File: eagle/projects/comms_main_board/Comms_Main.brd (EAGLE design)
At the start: 101.6 x 95.2 mm, 195 parts, among them J1 WRL-00593, J10 MOL-SL-2-RA, J11 MOL-SL-3-RA, J12 MOL-SL-3-RA, J13 MOL-SL-3-RA, J14 MOL-SL-3-RA, J15 MOL-SL-2-RA, J16 MOL-MINIJR-2P-RA, J17 MOL-MINIJR-2P-RA, J18 MOL-MINIJR-2P-RA, J19 MOL-MINIJR-2P-RA, J2 PRT-12639, J20 MOL-SL-2-RA, J21 RECEPTACLE-2x2-254MM, J22 MOL-SL-2-RA, J3 PRT-12639, J4 PRT-12639, J5 PRT-12639, J6 MOL-SL-3-RA, J7 MOL-SL-5-RA, J8 RECEPTACLE-2x20-254MM, J9 MOL-SL-3-RA, Q1 CSD17579Q3A, U1 TPS562209DDCT, U10 MCP4541-103E/MS, U11 TPS562209DDCT, U12 MMBT3904-HF, U13 MAX3232CSE+, U14 MAX4311, U15 MAX6371, U16 2N7002P,215, U2 LP2985-33DBVR, U3 LP5900TLX-3.3/NOPB, U4 TPS562209DDCT, U5 NDT2955, U6 LM3488MMX/NOPB, U7 PCT2075D,118, U8 MS560702BA03-50, U9 MAX-M8Q

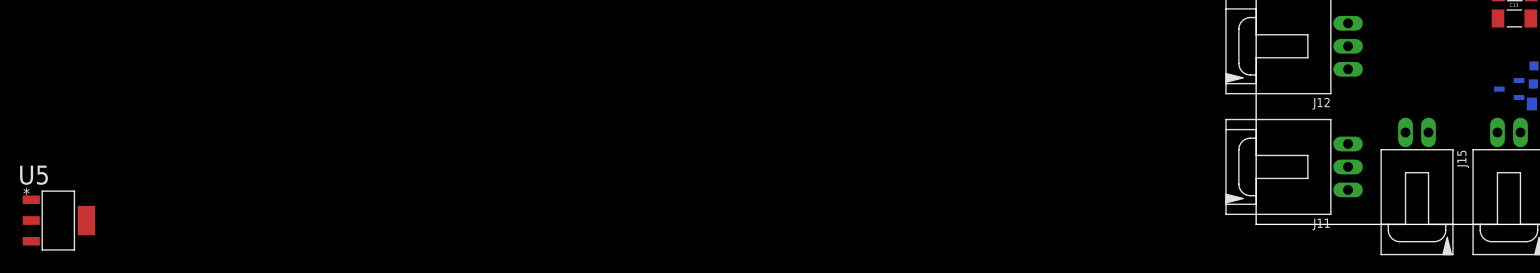
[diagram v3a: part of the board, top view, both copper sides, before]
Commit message: No-pop as assembly variant
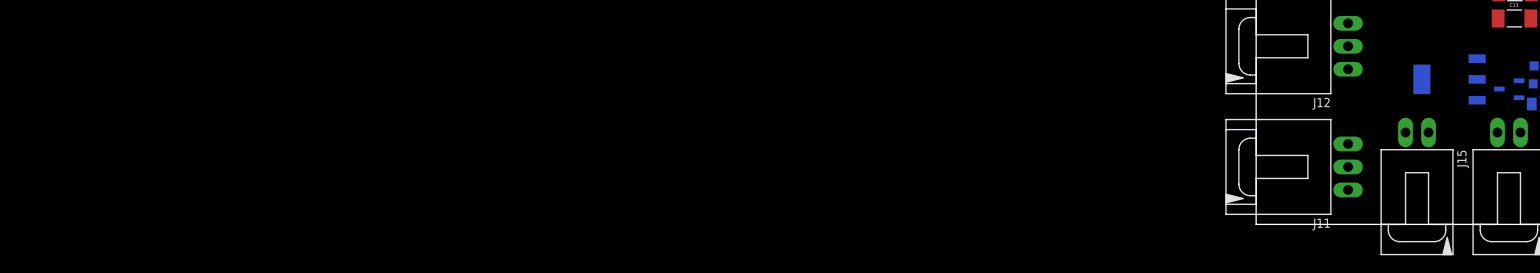
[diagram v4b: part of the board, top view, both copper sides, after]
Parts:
- moved U5 154.6 mm to (21.4, 16.0), flipped to the bottom
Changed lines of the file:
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@@
 </attributes>
 <variantdefs>
+<variantdef name="POR" current="yes"/>
 </variantdefs>
 <classes>
@@
 <attribute name="VENDOR" value="Digi-key" x="95.609096875" y="13.490184375" size="1.778" layer="28" rot="MR0" display="off"/>
 </element>
-<element name="R15" library="comms" package="R0603" value="0" x="95.6318625" y="15.678475" rot="MR0">
+<element name="R15" library="comms" package="R0603" value="0" x="95.6318625" y="15.678475" populate="no" rot="MR0">
 <attribute name="VENDOR_PN" value="P0.0GCT-ND" x="95.6318625" y="15.678475" size="1.778" layer="28" rot="MR0" display="off"/>
 <attribute name="MANUFACTURER_PN" value="ERJ-3GEY0R00V" x="95.6318625" y="15.678475" size="1.778" layer="28" rot="MR0" display="off"/>
@@
 <attribute name="VENDOR" value="Digi-key" x="32.831990625" y="28.757325" size="1.778" layer="27" display="off"/>
 </element>
-<element name="R20" library="comms" package="R0603" value="10k" x="31.856203125" y="76.851334375" rot="MR0">
+<element name="R20" library="comms" package="R0603" value="10k" x="31.856203125" y="76.851334375" populate="no" rot="MR0">
 <attribute name="VENDOR_PN" value="P10.0KHCT-ND" x="31.856203125" y="76.851334375" size="1.778" layer="28" rot="MR0" display="off"/>
 <attribute name="MANUFACTURER_PN" value="ERJ-3EKF1002V" x="31.856203125" y="76.851334375" size="1.778" layer="28" rot="MR0" display="off"/>
@@
 <attribute name="VENDOR" value="Digi-key" x="18.918459375" y="36.007771875" size="1.778" layer="28" rot="MR0" display="off"/>
 </element>
-<element name="R47" library="comms" package="R0603" value="0" x="18.70040625" y="40.48303125" rot="MR0">
+<element name="R47" library="comms" package="R0603" value="0" x="18.70040625" y="40.48303125" populate="no" rot="MR0">
 <attribute name="VENDOR_PN" value="P0.0GCT-ND" x="18.70040625" y="40.48303125" size="1.778" layer="28" rot="MR0" display="off"/>
 <attribute name="MANUFACTURER_PN" value="ERJ-3GEY0R00V" x="18.70040625" y="40.48303125" size="1.778" layer="28" rot="MR0" display="off"/>
@@
 <attribute name="VENDOR" value="Digi-key" x="18.992075" y="25.333253125" size="1.778" layer="28" rot="MR0" display="off"/>
 </element>
-<element name="R55" library="comms" package="R0805" value="0.0" x="39.84961875" y="68.887096875" rot="MR0">
+<element name="R55" library="comms" package="R0805" value="0.0" x="39.84961875" y="68.887096875" populate="no" rot="MR0">
 <attribute name="VENDOR_PN" value="P0.0ACT-ND" x="39.84961875" y="68.887096875" size="1.778" layer="28" rot="MR0" display="off"/>
 <attribute name="MANUFACTURER_PN" value="ERJ-6GEY0R00V" x="39.84961875" y="68.887096875" size="1.778" layer="28" rot="MR0" display="off"/>
@@
 <attribute name="VENDOR" value="Digi-Key" x="39.84961875" y="68.887096875" size="1.778" layer="28" rot="MR0" display="off"/>
 </element>
-<element name="R56" library="comms" package="R0805" value="0.0" x="54.45951875" y="69.015196875" rot="MR0">
+<element name="R56" library="comms" package="R0805" value="0.0" x="54.45951875" y="69.015196875" populate="no" rot="MR0">
 <attribute name="VENDOR_PN" value="P0.0ACT-ND" x="54.45951875" y="69.015196875" size="1.778" layer="28" rot="MR0" display="off"/>
 <attribute name="MANUFACTURER_PN" value="ERJ-6GEY0R00V" x="54.45951875" y="69.015196875" size="1.778" layer="28" rot="MR0" display="off"/>
@@
 <attribute name="VENDOR_PN" value="568-5818-1-ND" x="27.960040625" y="14.95311875" size="1.778" layer="28" rot="MR0" display="off"/>
 </element>
-<element name="R10" library="comms" package="R0805" value="0.0" x="31.463203125" y="13.299940625" rot="MR0">
+<element name="R10" library="comms" package="R0805" value="0.0" x="31.463203125" y="13.299940625" populate="no" rot="MR0">
 <attribute name="POWER" value="1/8W" x="31.463203125" y="13.299940625" size="1.778" layer="28" rot="MR0" display="off"/>
 <attribute name="VENDOR" value="Digi-Key" x="31.463203125" y="13.299940625" size="1.778" layer="28" rot="MR0" display="off"/>
@@
 <attribute name="VENDOR_PN" value="P0.0ACT-ND" x="31.463203125" y="13.299940625" size="1.778" layer="28" rot="MR0" display="off"/>
 </element>
-<element name="U5" library="comms" package="SOT230P700X180-4N" value="NDT2955" x="-132.375821875" y="0.4259625">
-<attribute name="VENDOR_PN" value="NDT2955CT-ND" x="-132.375821875" y="0.4259625" size="1.778" layer="27" display="off"/>
-<attribute name="VENDOR" value="Digi-Key" x="-132.375821875" y="0.4259625" size="1.778" layer="27" display="off"/>
-<attribute name="MANUFACTURER" value="Fairchild" x="-132.375821875" y="0.4259625" size="1.778" layer="27" display="off"/>
-<attribute name="MANUFACTURER_PN" value="NDT2955" x="-132.375821875" y="0.4259625" size="1.778" layer="27" display="off"/>
-<attribute name="PACKAGE" value="SOT-223-4" x="-132.375821875" y="0.4259625" size="1.778" layer="27" display="off"/>
+<element name="U5" library="comms" package="SOT230P700X180-4N" value="NDT2955" x="21.41910625" y="16.024090625" rot="MR0">
+<attribute name="VENDOR_PN" value="NDT2955CT-ND" x="21.41910625" y="16.024090625" size="1.778" layer="28" rot="MR0" display="off"/>
+<attribute name="VENDOR" value="Digi-Key" x="21.41910625" y="16.024090625" size="1.778" layer="28" rot="MR0" display="off"/>
+<attribute name="MANUFACTURER" value="Fairchild" x="21.41910625" y="16.024090625" size="1.778" layer="28" rot="MR0" display="off"/>
+<attribute name="MANUFACTURER_PN" value="NDT2955" x="21.41910625" y="16.024090625" size="1.778" layer="28" rot="MR0" display="off"/>
+<attribute name="PACKAGE" value="SOT-223-4" x="21.41910625" y="16.024090625" size="1.778" layer="28" rot="MR0" display="off"/>
 </element>
 </elements>
@@
 <contactref element="R8" pad="2"/>
 <contactref element="U5" pad="3"/>
-<wire x1="-24.13" y1="114.3" x2="-135.375821875" y2="-1.8740375" width="0" layer="19" extent="1-1"/>
-<wire x1="55.43383125" y1="59.4553" x2="-24.13" y2="114.3" width="0" layer="19" extent="1-1"/>
-<wire x1="65.582725" y1="55.370571875" x2="55.43383125" y2="59.4553" width="0" layer="19" extent="1-1"/>
-<wire x1="69.892540625" y1="54.175978125" x2="65.582725" y2="55.370571875" width="0" layer="19" extent="1-1"/>
+<wire x1="65.582725" y1="55.370571875" x2="69.892540625" y2="54.175978125" width="0" layer="19" extent="1-1"/>
+<wire x1="55.43383125" y1="59.4553" x2="65.582725" y2="55.370571875" width="0" layer="19" extent="1-1"/>
 <wire x1="71.755" y1="13.97" x2="69.892540625" y2="54.175978125" width="0" layer="19" extent="1-1"/>
 <wire x1="30.713996875" y1="17.52249375" x2="71.755" y2="13.97" width="0" layer="19" extent="16-16"/>
 <wire x1="30.463203125" y1="13.299940625" x2="30.713996875" y2="17.52249375" width="0" layer="19" extent="16-16"/>
+<wire x1="24.41910625" y1="13.724090625" x2="30.463203125" y2="13.299940625" width="0" layer="19" extent="16-16"/>
+<wire x1="-24.13" y1="114.3" x2="55.43383125" y2="59.4553" width="0" layer="19" extent="1-1"/>
 </signal>
 <signal name="DCDC_STEPUP_ISENSE_RES">
@@
 <contactref element="U5" pad="2"/>
 <contactref element="U5" pad="4"/>
-<wire x1="-129.275821875" y1="0.4259625" x2="-135.375821875" y2="0.4259625" width="0" layer="19" extent="1-1"/>
-<wire x1="32.463203125" y1="13.299940625" x2="-129.275821875" y2="0.4259625" width="0" layer="19" extent="1-16"/>
-<wire x1="39.37" y1="10.16" x2="32.463203125" y2="13.299940625" width="0" layer="19" extent="16-16"/>
+<wire x1="32.463203125" y1="13.299940625" x2="39.37" y2="10.16" width="0" layer="19" extent="16-16"/>
+<wire x1="24.41910625" y1="16.024090625" x2="32.463203125" y2="13.299940625" width="0" layer="19" extent="16-16"/>
+<wire x1="18.31910625" y1="16.024090625" x2="24.41910625" y2="16.024090625" width="0" layer="19" extent="16-16"/>
 </signal>
 <signal name="12V_PMOS_G">
@@
 <contactref element="U16" pad="3"/>
 <contactref element="U5" pad="1"/>
-<wire x1="26.867840625" y1="14.95311875" x2="-135.375821875" y2="2.7259625" width="0" layer="19" extent="1-16"/>
-<wire x1="32.413996875" y1="17.52249375" x2="26.867840625" y2="14.95311875" width="0" layer="19" extent="16-16"/>
+<wire x1="26.867840625" y1="14.95311875" x2="32.413996875" y2="17.52249375" width="0" layer="19" extent="16-16"/>
+<wire x1="24.41910625" y1="18.324090625" x2="26.867840625" y2="14.95311875" width="0" layer="19" extent="16-16"/>
 </signal>
 </signals>

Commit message: Changed WDT to be off 3.3V rail
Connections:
- net 3P3V_SENSORS: now also C36.1, R19.1, R20.2, U15.4, U15.5, U15.8
- net 5V_PI: no longer C36.1, R19.1, R20.2, U15.4, U15.5, U15.8
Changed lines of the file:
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@@
 <contactref element="U8" pad="2"/>
 <contactref element="R55" pad="2"/>
+<contactref element="U15" pad="5"/>
+<contactref element="U15" pad="4"/>
+<contactref element="U15" pad="8"/>
+<contactref element="C36" pad="1"/>
+<contactref element="R19" pad="1"/>
+<contactref element="R20" pad="2"/>
 <wire x1="57.640990625" y1="68.277221875" x2="57.216571875" y2="72.097946875" width="0" layer="19" extent="16-16"/>
 <wire x1="56.27350625" y1="66.3569625" x2="57.640990625" y2="68.277221875" width="0" layer="19" extent="16-16"/>
@@
 <wire x1="37.07379375" y1="69.094459375" x2="38.84961875" y2="68.887096875" width="0" layer="19" extent="16-16"/>
 <wire x1="37.07379375" y1="67.844459375" x2="37.07379375" y2="69.094459375" width="0" layer="19" extent="16-16"/>
+<wire x1="31.006203125" y1="76.851334375" x2="38.410153125" y2="71.502978125" width="0" layer="19" extent="16-16"/>
+<wire x1="29.3049625" y1="75.661178125" x2="31.006203125" y2="76.851334375" width="0" layer="19" extent="16-16"/>
+<wire x1="29.092090625" y1="73.712196875" x2="29.3049625" y2="75.661178125" width="0" layer="19" extent="16-16"/>
+<wire x1="26.9549625" y1="75.661178125" x2="29.3049625" y2="75.661178125" width="0" layer="19" extent="16-16"/>
+<wire x1="26.9549625" y1="77.611178125" x2="26.9549625" y2="75.661178125" width="0" layer="19" extent="16-16"/>
+<wire x1="32.644853125" y1="78.86829375" x2="31.006203125" y2="76.851334375" width="0" layer="19" extent="16-16"/>
 <wire x1="27.636603125" y1="54.31660625" x2="37.07379375" y2="67.844459375" width="0" layer="19" extent="16-16"/>
 <wire x1="28.364871875" y1="47.547296875" x2="27.636603125" y2="54.31660625" width="0" layer="19" extent="1-16"/>
@@
 </signal>
 <signal name="5V_PI">
-<contactref element="U15" pad="5"/>
-<contactref element="U15" pad="4"/>
-<contactref element="U15" pad="8"/>
-<contactref element="C36" pad="1"/>
-<contactref element="R19" pad="1"/>
-<contactref element="R20" pad="2"/>
 <contactref element="R1" pad="2"/>
 <contactref element="C3" pad="1"/>
@@
 <contactref element="J8" pad="2"/>
 <contactref element="J8" pad="4"/>
-<wire x1="31.006203125" y1="76.851334375" x2="32.644853125" y2="78.86829375" width="0" layer="19" extent="16-16"/>
-<wire x1="29.3049625" y1="75.661178125" x2="31.006203125" y2="76.851334375" width="0" layer="19" extent="16-16"/>
-<wire x1="29.092090625" y1="73.712196875" x2="29.3049625" y2="75.661178125" width="0" layer="19" extent="16-16"/>
-<wire x1="26.9549625" y1="75.661178125" x2="29.3049625" y2="75.661178125" width="0" layer="19" extent="16-16"/>
-<wire x1="26.9549625" y1="77.611178125" x2="26.9549625" y2="75.661178125" width="0" layer="19" extent="16-16"/>
-<wire x1="13.97" y1="86.36" x2="26.9549625" y2="77.611178125" width="0" layer="19" extent="16-16"/>
 <wire x1="11.43" y1="86.36" x2="13.97" y2="86.36" width="0" layer="19" extent="1-1"/>
-<wire x1="36.364071875" y1="33.68104375" x2="29.092090625" y2="73.712196875" width="0" layer="19" extent="1-16"/>
+<wire x1="36.364071875" y1="33.68104375" x2="13.97" y2="86.36" width="0" layer="19" extent="1-1"/>
 <wire x1="37.620825" y1="26.911371875" x2="36.364071875" y2="33.68104375" width="0" layer="19" extent="1-1"/>
 <wire x1="26.79621875" y1="25.651803125" x2="37.620825" y2="26.911371875" width="0" layer="19" extent="1-1"/>

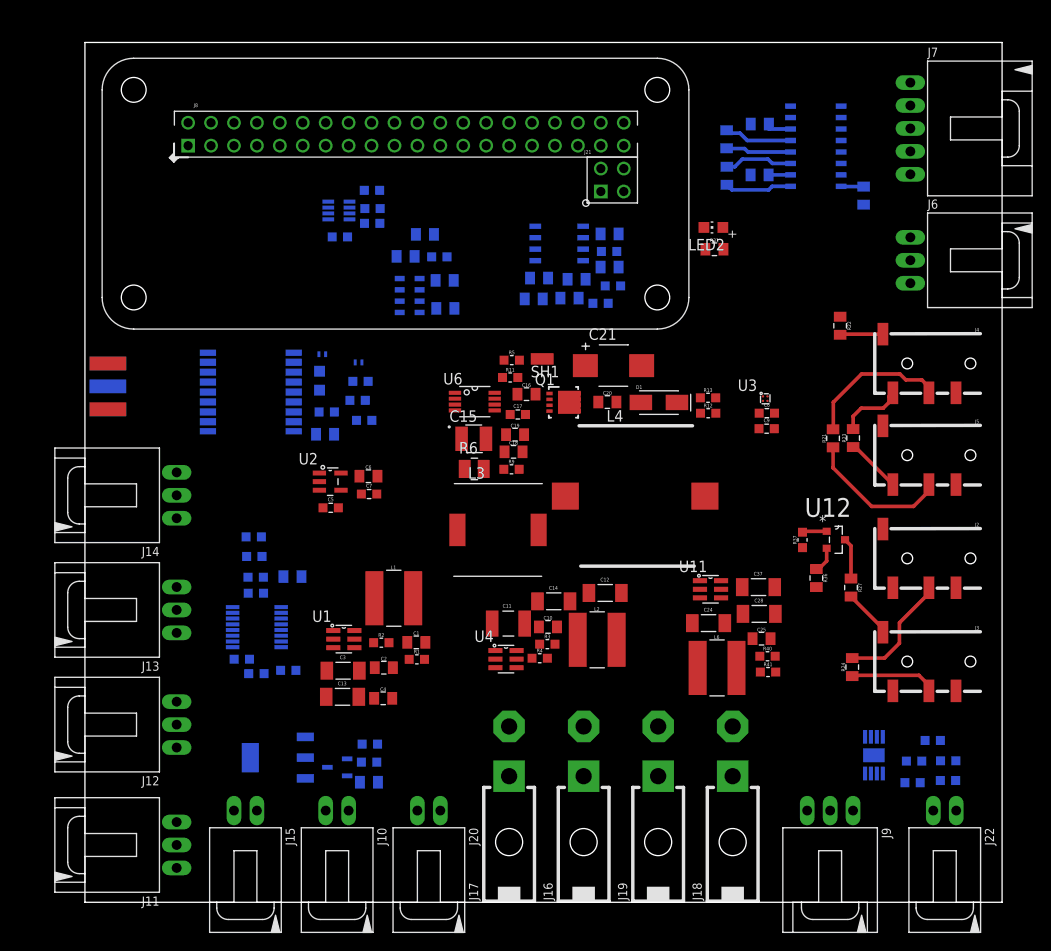
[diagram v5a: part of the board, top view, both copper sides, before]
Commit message: Update inductor
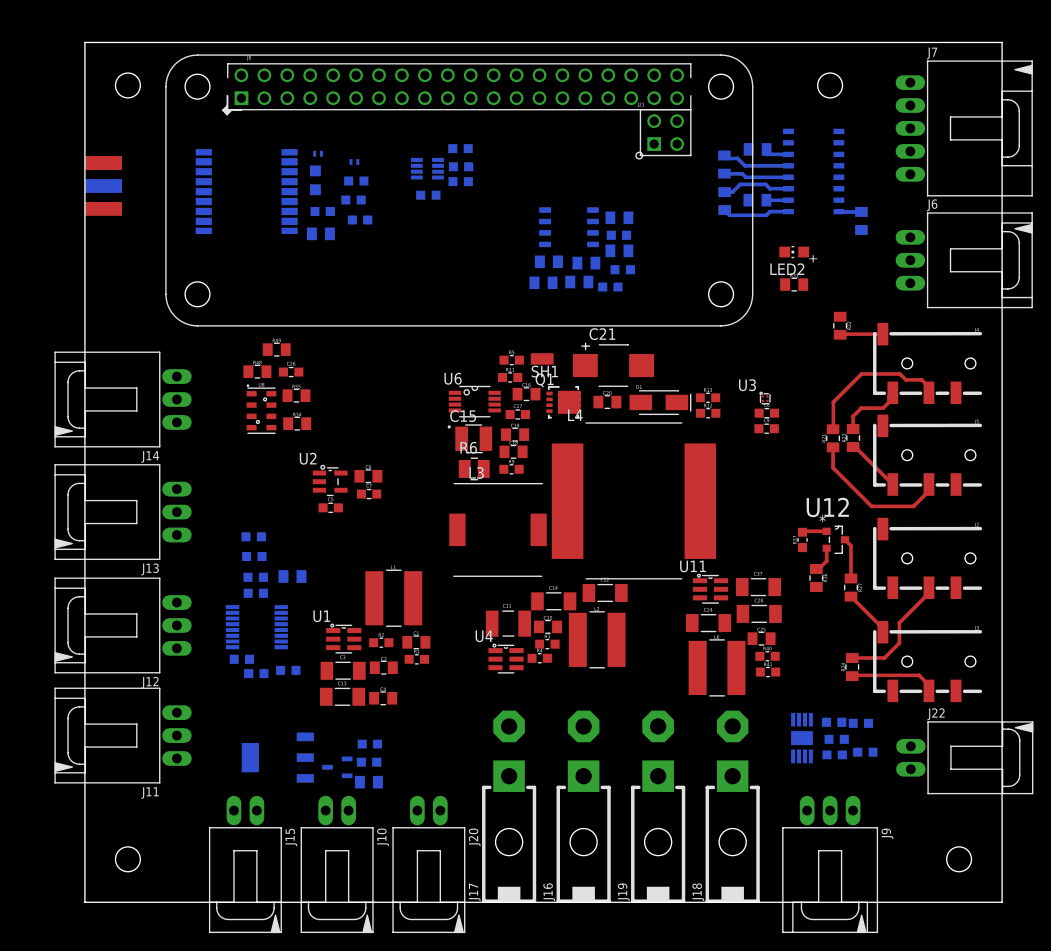
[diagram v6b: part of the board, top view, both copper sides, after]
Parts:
- added H1, H2, H3, H4: MOUNT-HOLE_2.75, comms:2,75_HOLE_RASPI
- L4: value 47uH -> 68uH; device comms:ASPI-1306T -> comms:HCMA1707
- moved R17 22.2 mm to (30.1, 79.9)
- moved FB2 22.2 mm to (25.8, 82.9)
- moved J1 22.2 mm to (2.08, 76.8)
- moved R16 22.2 mm to (29.7, 77.8)
- moved U9 22.2 mm to (18.1, 78.8)
- moved C22 22.2 mm to (26.1, 74.1)
- moved C27 22.2 mm to (26.3, 76.5)
- moved FB1 22.2 mm to (29.9, 82.0)
- moved L5 22.2 mm to (30.5, 75.6)
- moved LED1 22.2 mm to (25.5, 80.0)
- moved R49 20.8 mm to (21.2, 61.2), flipped to the top
- moved C26 20.8 mm to (22.8, 58.7), flipped to the top
- moved R48 20.8 mm to (19.1, 58.8), flipped to the top
- moved U8 20.8 mm to (19.6, 54.5), flipped to the top
- moved R34 20.8 mm to (23.5, 53.0), flipped to the top
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
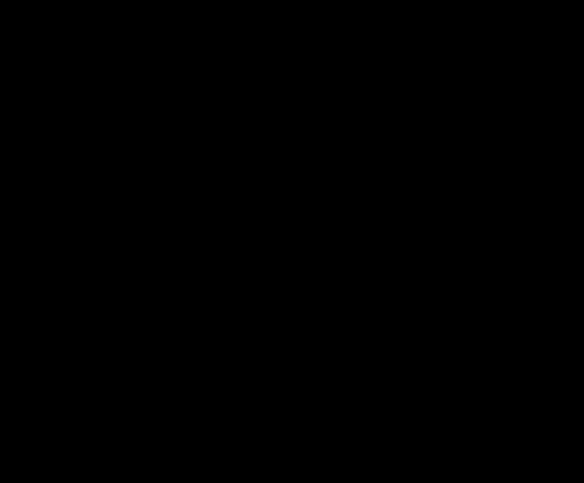
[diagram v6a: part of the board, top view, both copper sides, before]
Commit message: Added ground test points
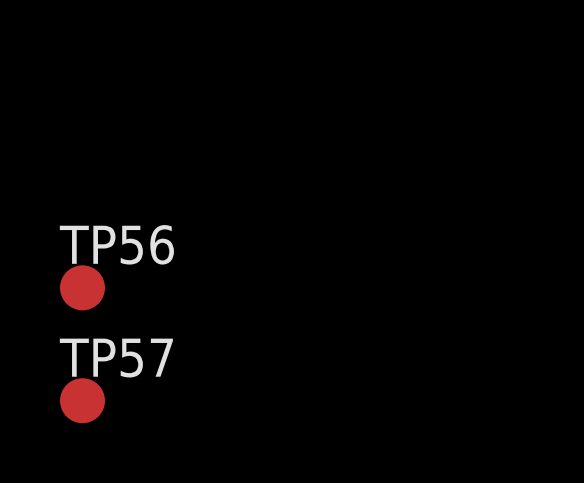
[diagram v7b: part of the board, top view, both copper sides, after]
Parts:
- added TP56, TP57: TPTP15R, comms:TP15R
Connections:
- net GND: now also TP56.TP, TP57.TP
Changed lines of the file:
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@@
 <attribute name="CURRENT_SAT" value="6.5A" x="60.81888125" y="44.432390625" size="1.778" layer="27" display="off"/>
+</element>
+<element name="TP56" library="comms" package="TP15R" value="TPTP15R" x="-123.19" y="-7.0619625">
+<attribute name="TP_SIGNAL_NAME" value="" x="-123.19" y="-7.0619625" size="1.778" layer="27" display="off"/>
+</element>
+<element name="TP57" library="comms" package="TP15R" value="TPTP15R" x="-123.19" y="-10.82539375">
+<attribute name="TP_SIGNAL_NAME" value="" x="-123.19" y="-10.82539375" size="1.778" layer="27" display="off"/>
 </element>
 </elements>
@@
 <contactref element="U16" pad="2"/>
 <contactref element="L4" pad="2"/>
+<contactref element="TP56" pad="TP"/>
+<contactref element="TP57" pad="TP"/>
 <wire x1="83.52305625" y1="80.316190625" x2="91.44" y2="80.645" width="0" layer="19" extent="16-16"/>
 <wire x1="83.52305625" y1="77.776190625" x2="83.52305625" y2="80.316190625" width="0" layer="19" extent="16-16"/>
@@
 <wire x1="96.495" y1="34.85" x2="88.395" y2="41.35" width="0" layer="19" extent="1-1"/>
 <wire x1="-119.38" y1="110.49" x2="2.0787125" y2="81.892746875" width="0" layer="19" extent="1-16"/>
+<wire x1="-123.19" y1="-7.0619625" x2="-119.38" y2="110.49" width="0" layer="19" extent="1-1"/>
+<wire x1="-123.19" y1="-10.82539375" x2="-123.19" y2="-7.0619625" width="0" layer="19" extent="1-1"/>
 </signal>
 <signal name="7P4V_IN">
